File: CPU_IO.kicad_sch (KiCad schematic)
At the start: 11 parts, among them SW1 Interrupt, U13D601 Z8530, U15D601 6522, U4E601 68000D, U601 Apple_IWM

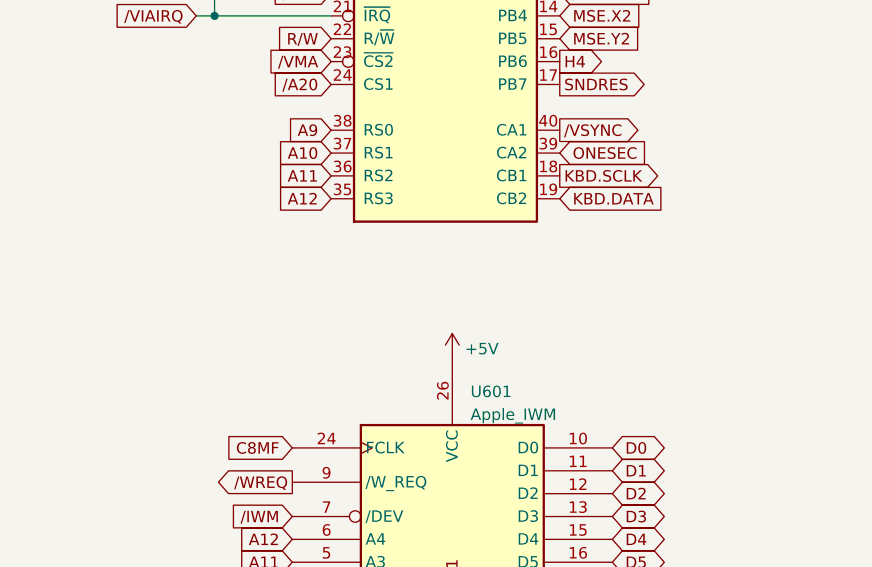
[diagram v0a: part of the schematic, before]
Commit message: Add files via upload
After obtaining actual  128k board, certain component placement tweaks were made. Board was re-routed based on those changes.
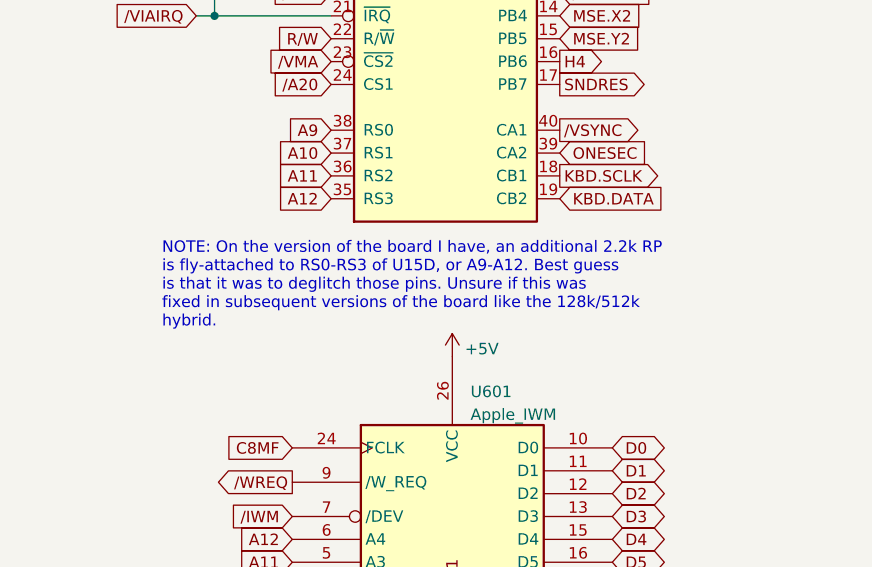
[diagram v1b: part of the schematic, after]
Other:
- note added: "NOTE: On the version of the board I have, an additional 2.2k RP is fly-attached to RS0-RS3 of U15D, or A9-A12. Best guess is that it was to deglitch those pins. Unsure if this was fixed in subsequent versions of the board like the 128k/512k hybrid."
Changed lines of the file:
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@@
+    (effects (font (size 1.27 1.27)) (justify left bottom))
+  )
+  (text "NOTE: On the version of the board I have, an additional 2.2k RP\nis fly-attached to RS0-RS3 of U15D, or A9-A12. Best guess\nis that it was to deglitch those pins. Unsure if this was\nfixed in subsequent versions of the board like the 128k/512k\nhybrid."
+    (at 217.678 96.266 0)
     (effects (font (size 1.27 1.27)) (justify left bottom))
   )
